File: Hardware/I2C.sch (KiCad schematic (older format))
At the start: 8 parts, among them J16 I2C 5V, J17 PPS, J6 I2C 3.3V, J8 I2C 3.3V, U4 BSS138, U5 BSS138

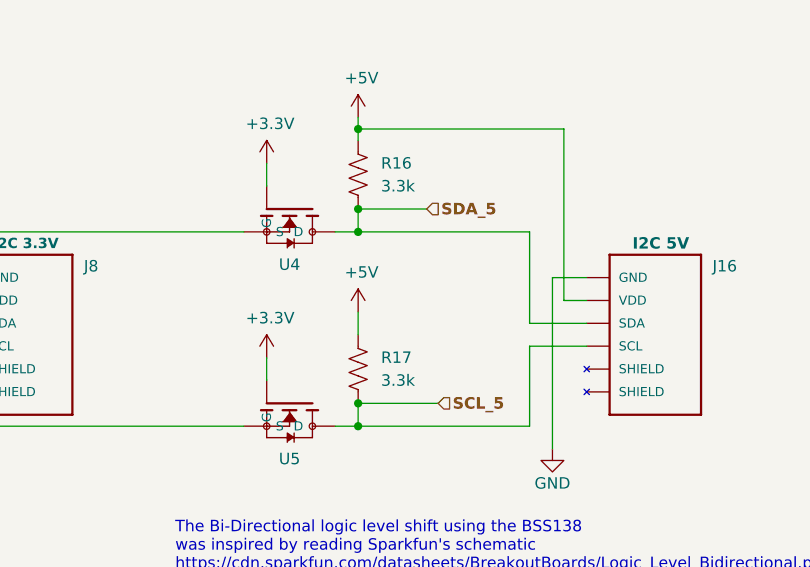
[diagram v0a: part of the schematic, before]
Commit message: Update PCB to latest schematic changes.
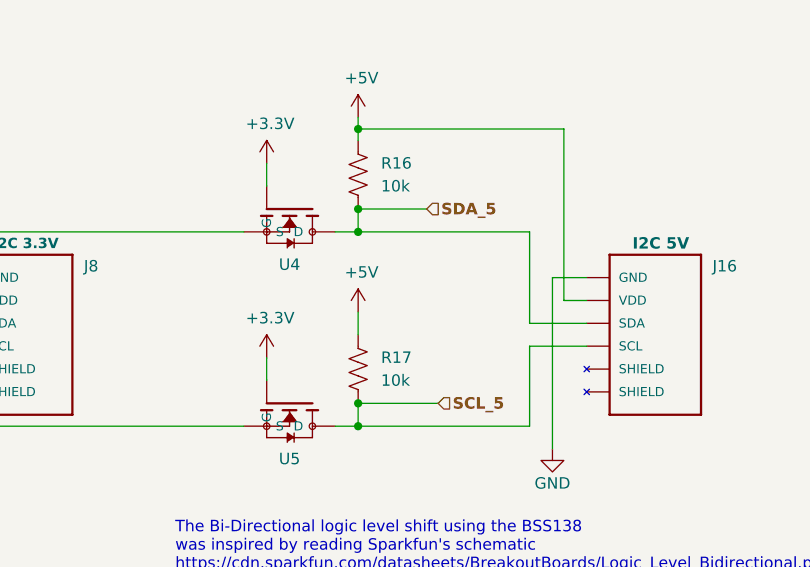
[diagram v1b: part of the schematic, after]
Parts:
- R16, R17: value 3.3k -> 10k
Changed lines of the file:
@@
 P 7100 4100
 F 0 "R17" H 7200 4150 50  0000 L CNN
-F 1 "3.3k" H 7200 4050 50  0000 L CNN
+F 1 "10k" H 7200 4050 50  0000 L CNN
 F 2 "Resistor_SMD:R_0805_2012Metric" V 7140 4090 50  0001 C CNN
 F 3 "~" H 7100 4100 50  0001 C CNN
@@
 P 7100 3250
 F 0 "R16" H 7200 3300 50  0000 L CNN
-F 1 "3.3k" H 7200 3200 50  0000 L CNN
+F 1 "10k" H 7200 3200 50  0000 L CNN
 F 2 "Resistor_SMD:R_0805_2012Metric" V 7140 3240 50  0001 C CNN
 F 3 "~" H 7100 3250 50  0001 C CNN
